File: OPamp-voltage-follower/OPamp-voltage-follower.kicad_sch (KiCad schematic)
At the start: 4 parts, among them U1 ${SIM.PARAMS}

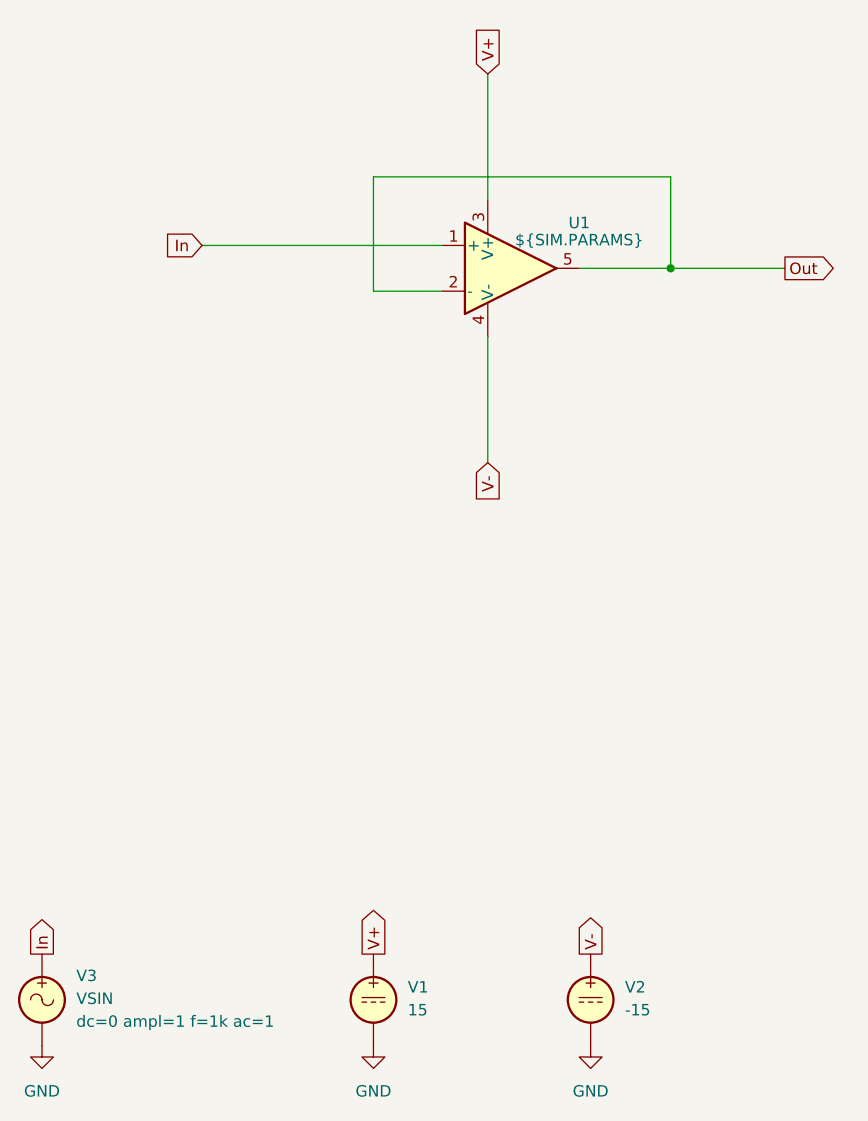
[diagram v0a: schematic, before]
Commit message: Tested/updated for KiCad 9
Schematics are tested and updated for KiCad 9, no changes in circuitry
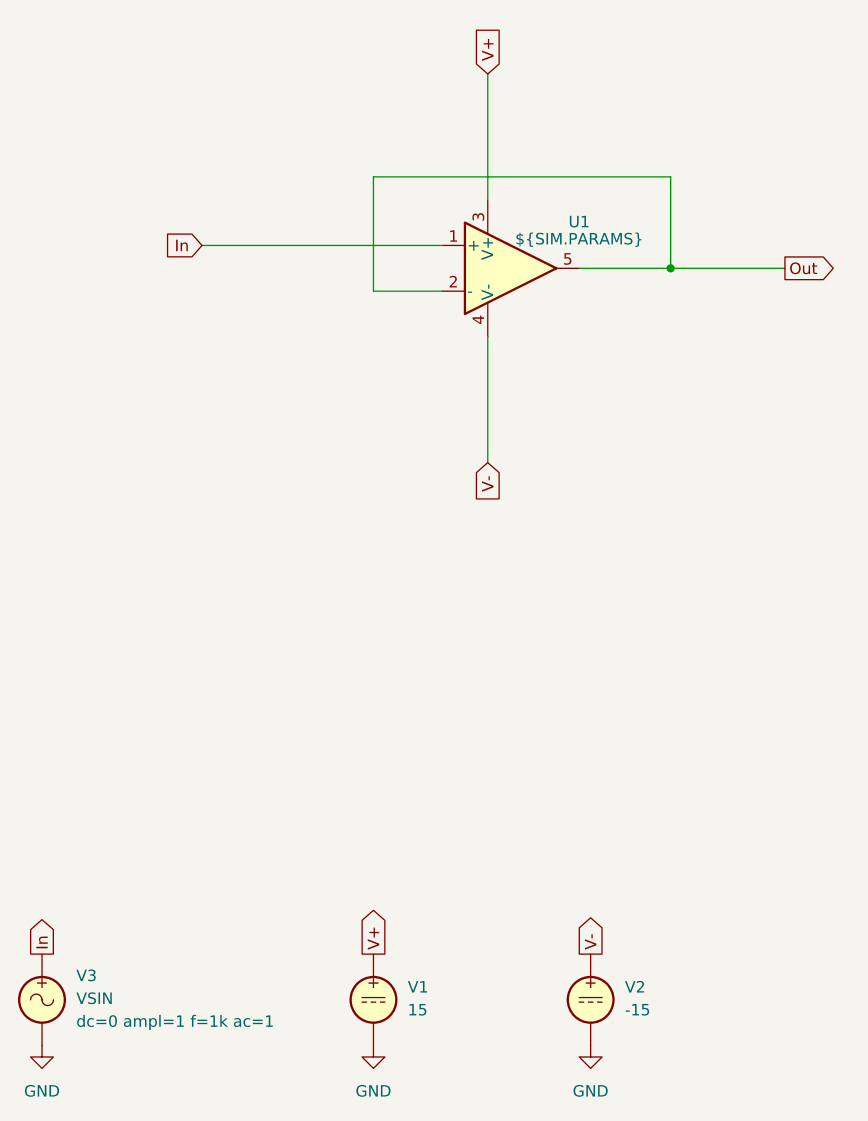
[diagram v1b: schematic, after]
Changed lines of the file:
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@@
 (kicad_sch
-	(version 20231120)
+	(version 20250114)
 	(generator "eeschema")
-	(generator_version "8.0")
+	(generator_version "9.0")
 	(paper "A4")
 	(title_block
 		(title "OPamp, voltage follower")
-		(date "2024-12-15")
+		(date "2025-09-13")
 		(company "GitHub/OJStuff")
 	)
@@
 	)
 	(symbol
-		(lib_id "Simulation_SPICE:OPAMP")
-		(at 151.13 100.33 0)
-		(unit 1)
-		(exclude_from_sim no)
-		(in_bom yes)
-		(on_board yes)
-		(dnp no)
-		(fields_autoplaced yes)
-		(property "Reference" "U1"
-			(at 158.75 95.2814 0)
-			(effects
-				(font
-					(size 1.27 1.27)
-				)
-			)
-		)
-		(property "Value" "${SIM.PARAMS}"
-			(at 158.75 97.1865 0)
-			(effects
-				(font
-					(size 1.27 1.27)
-				)
-			)
-		)
-		(property "Footprint" ""
-			(at 151.13 100.33 0)
-			(effects
-				(font
-					(size 1.27 1.27)
-				)
-				(hide yes)
-			)
-		)
-		(property "Datasheet" "https://ngspice.sourceforge.io/docs/ngspice-html-manual/manual.xhtml#sec__SUBCKT_Subcircuits"
-			(at 151.13 100.33 0)
-			(effects
-				(font
-					(size 1.27 1.27)
-				)
-				(hide yes)
-			)
-		)
-		(property "Description" "Operational amplifier, single, node sequence=1:+ 2:- 3:OUT 4:V+ 5:V-"
-			(at 151.13 100.33 0)
-			(effects
-				(font
-					(size 1.27 1.27)
-				)
-				(hide yes)
-			)
-		)
-		(property "Sim.Pins" "1=in+ 2=in- 3=vcc 4=vee 5=out"
-			(at 151.13 100.33 0)
-			(effects
-				(font
-					(size 1.27 1.27)
-				)
-				(hide yes)
-			)
-		)
-		(property "Sim.Device" "SUBCKT"
-			(at 151.13 100.33 0)
-			(effects
-				(font
-					(size 1.27 1.27)
-				)
-				(justify left)
-				(hide yes)
-			)
-		)
-		(property "Sim.Library" "${KICAD8_SYMBOL_DIR}/Simulation_SPICE.sp"
-			(at 151.13 100.33 0)
-			(effects
-				(font
-					(size 1.27 1.27)
-				)
-				(hide yes)
-			)
-		)
-		(property "Sim.Name" "kicad_builtin_opamp"
-			(at 151.13 100.33 0)
-			(effects
-				(font
-					(size 1.27 1.27)
-				)
-				(hide yes)
-			)
-		)
-		(pin "1"
-		)
-		(pin "3"
-		)
-		(pin "2"
-		)
-		(pin "5"
-		)
-		(pin "4"
-		)
-		(instances
-			(project ""
-				(path "/0e61ef13-cf31-4701-bd30-de17a8eacd55"
-					(reference "U1")
-					(unit 1)
-				)
-			)
-		)
-	)
-	(symbol
 		(lib_name "VDC_1")
 		(lib_id "Simulation_SPICE:VDC")
@@
 	)
 	(symbol
+		(lib_id "Simulation_SPICE:OPAMP")
+		(at 151.13 100.33 0)
+		(unit 1)
+		(exclude_from_sim no)
+		(in_bom yes)
+		(on_board yes)
+		(dnp no)
+		(fields_autoplaced yes)
+		(property "Reference" "U1"
+			(at 158.75 95.1798 0)
+			(effects
+				(font
+					(size 1.27 1.27)
+				)
+			)
+		)
+		(property "Value" "${SIM.PARAMS}"
+			(at 158.75 97.0849 0)
+			(effects
+				(font
+					(size 1.27 1.27)
+				)
+			)
+		)
+		(property "Footprint" ""
+			(at 151.13 100.33 0)
+			(effects
+				(font
+					(size 1.27 1.27)
+				)
+				(hide yes)
+			)
+		)
+		(property "Datasheet" "https://ngspice.sourceforge.io/docs/ngspice-html-manual/manual.xhtml#sec__SUBCKT_Subcircuits"
+			(at 151.13 100.33 0)
+			(effects
+				(font
+					(size 1.27 1.27)
+				)
+				(hide yes)
+			)
+		)
+		(property "Description" "Operational amplifier, single"
+			(at 151.13 100.33 0)
+			(effects
+				(font
+					(size 1.27 1.27)
+				)
+				(hide yes)
+			)
+		)
+		(property "Sim.Pins" "1=in+ 2=in- 3=vcc 4=vee 5=out"
+			(at 151.13 100.33 0)
+			(effects
+				(font
+					(size 1.27 1.27)
+				)
+				(hide yes)
+			)
+		)
+		(property "Sim.Device" "SUBCKT"
+			(at 151.13 100.33 0)
+			(effects
+				(font
+					(size 1.27 1.27)
+				)
+				(justify left)
+				(hide yes)
+			)
+		)
+		(property "Sim.Library" "${KICAD9_SYMBOL_DIR}/Simulation_SPICE.sp"
+			(at 151.13 100.33 0)
+			(effects
+				(font
+					(size 1.27 1.27)
+				)
+				(hide yes)
+			)
+		)
+		(property "Sim.Name" "kicad_builtin_opamp"
+			(at 151.13 100.33 0)
+			(effects
+				(font
+					(size 1.27 1.27)
+				)
+				(hide yes)
+			)
+		)
+		(pin "1"
+		)
+		(pin "2"
+		)
+		(pin "3"
+		)
+		(pin "4"
+		)
+		(pin "5"
+		)
+		(instances
+			(project ""
+				(path "/0e61ef13-cf31-4701-bd30-de17a8eacd55"
+					(reference "U1")
+					(unit 1)
+				)
+			)
+		)
+	)
+	(symbol
 		(lib_id "power:GND")
 		(at 135.89 186.69 0)
@@
 		)
 	)
+	(embedded_fonts no)
 )
